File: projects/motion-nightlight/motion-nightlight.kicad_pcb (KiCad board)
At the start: 2 copper layers, 48 x 50 mm, 19 parts, among them Q1 DARK_NPN_EBC, Q2 LED_CONTROL_NPN, SW1 SW_Push, SW2 SENSOR, SW3 MODE, U1 74HC14, U2 74LS08

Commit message: clean ERC and DRC
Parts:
- moved LED1 26.8 mm to (156.5, 72.0)
- moved C1 23.0 mm to (154.0, 107.5), turned to -90 degrees
- moved SW1 22.9 mm to (158.8, 94.2), turned to -90 degrees
- moved R1 15.9 mm to (117.0, 99.5), turned to 0 degrees
- moved C2 15.7 mm to (159.0, 107.5), turned to -90 degrees
- moved LDR1 8.70 mm to (117.0, 94.5), turned to 0 degrees
- moved R2 8.40 mm to (117.0, 104.6), turned to 0 degrees
- moved R_B1 7.00 mm to (138.0, 77.3), turned to 90 degrees
- moved R_PD1 6.98 mm to (130.5, 77.3), turned to 90 degrees
- moved R3 5.68 mm to (124.7, 109.7)
- moved RV1 4.01 mm to (123.4, 89.5)
- moved PIR1 4.00 mm to (145.5, 82.9)
- moved SW3 3.20 mm to (156.2, 83.5)
- moved U1 1.63 mm to (129.2, 94.4)
- moved U2 1.63 mm to (141.7, 94.4)
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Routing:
- net /LED_ON: track 66.7 -> 9.89 mm
- net +3.3V: track 179.4 -> 156.1 mm
- net /AND_ON: track 21.1 -> 33.6 mm
- net /DARK_RAW: track 39.6 -> 27.3 mm
- net /SENSOR_DIG: track 23.3 -> 34.4 mm
- net Net-(Q1-B): track 26.3 -> 34.0 mm
- net /MOTION_RAW: track 9.38 -> 12.8 mm
- net Net-(LDR1-Pad2): track 21.2 -> 23.6 mm
- net /MOTION_DIG: track 41.7 -> 39.5 mm
- net /DARK_DIG: track 46.5 -> 48.6 mm
- net /LIGHT_ON: track 38.1 -> 38.8 mm
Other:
- board size 48 x 50 mm -> 46.7 x 45.8 mm
- board text added: "&"
- board text added: "S"
- board text removed: "AND"
- board text removed: "SENSOR"

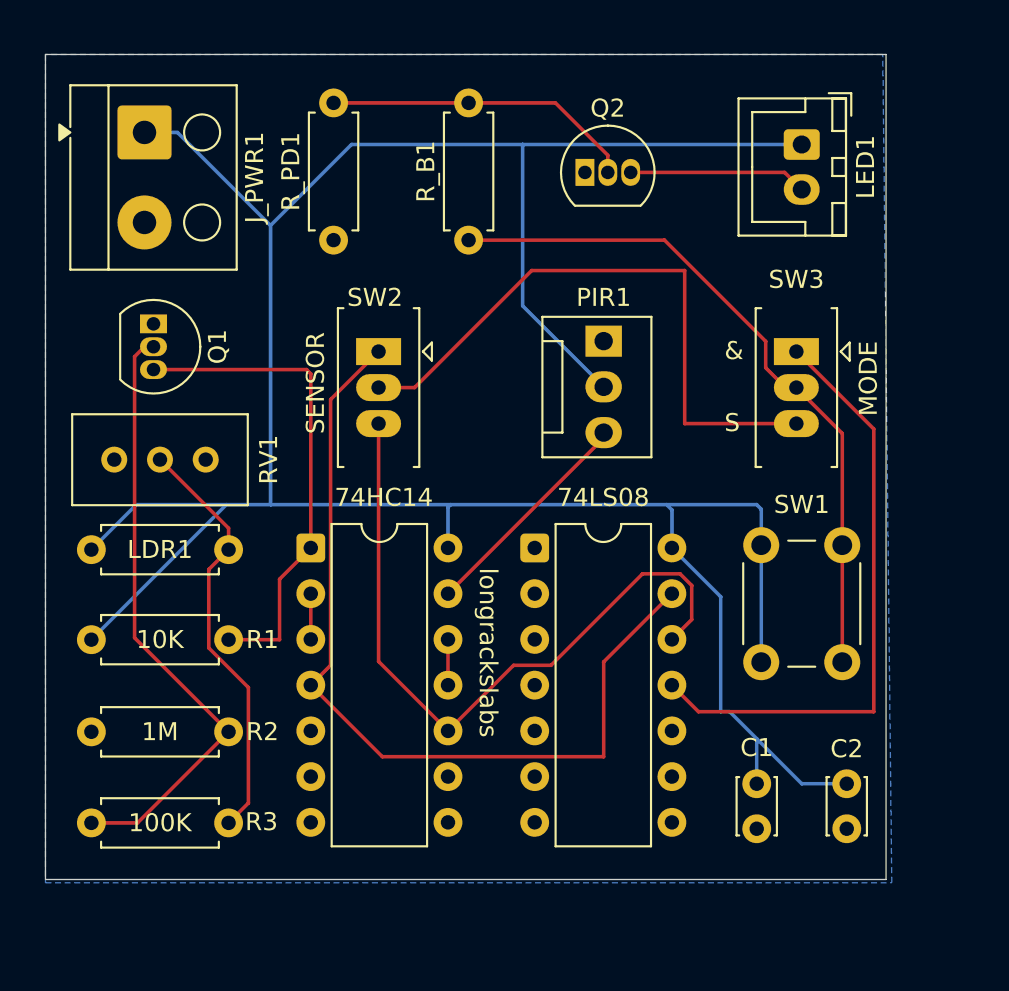
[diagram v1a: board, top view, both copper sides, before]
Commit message: layout tweaks for caps
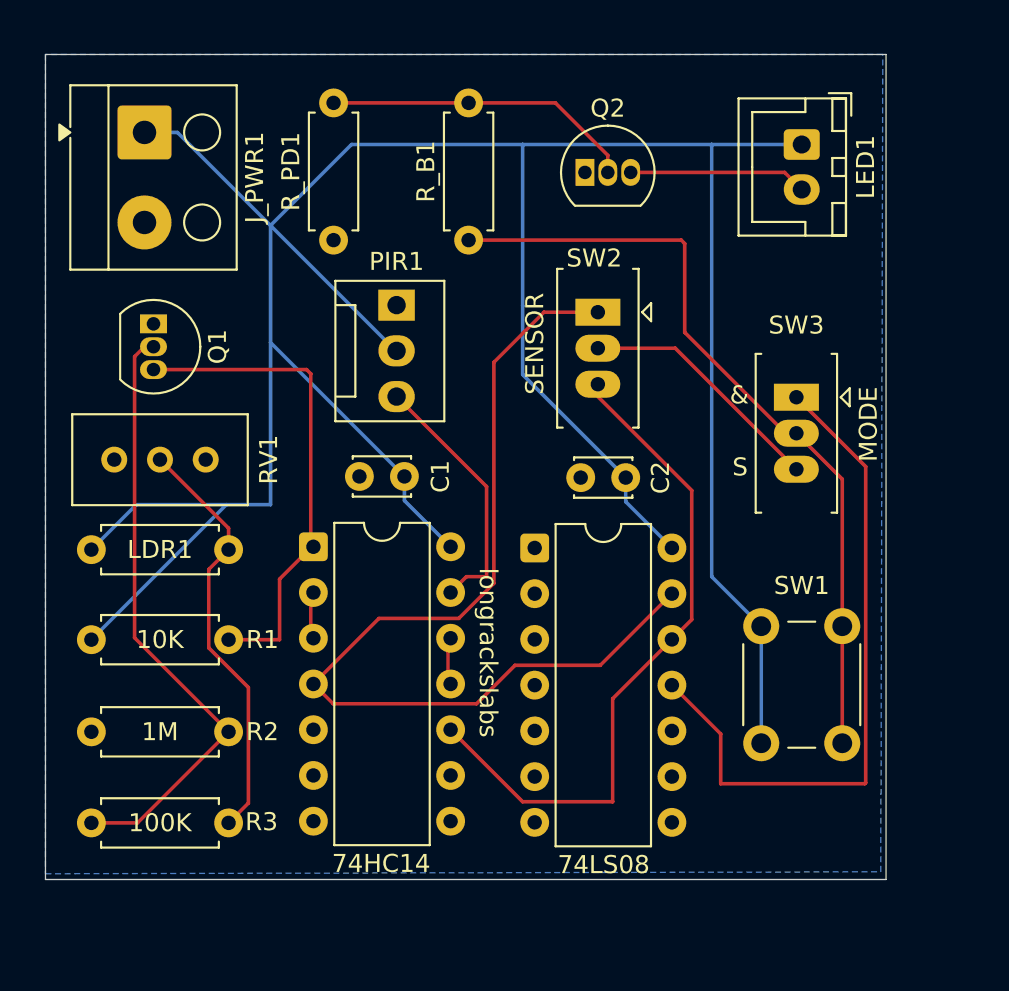
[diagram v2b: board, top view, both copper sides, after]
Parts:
- moved C1 26.0 mm to (134.4, 90.4), turned to 180 degrees
- moved C2 21.0 mm to (146.7, 90.5), turned to 180 degrees
- moved SW2 12.4 mm to (145.2, 81.3)
- moved PIR1 11.7 mm to (134.0, 80.9)
- moved SW1 4.50 mm to (158.8, 98.8)
- moved SW3 2.54 mm to (156.2, 86.0)
- moved U1 0.16 mm to (129.4, 94.3)
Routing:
- net /SENSOR_DIG: track 34.4 -> 13.8 mm
- net +3.3V: track 156.1 -> 164.1 mm
- net /DARK_DIG: track 48.6 -> 54.4 mm
- net /LIGHT_ON: track 38.8 -> 43.8 mm
- net /AND_ON: track 33.6 -> 38.3 mm
- net /MOTION_DIG: track 39.5 -> 37.1 mm
- net /MOTION_RAW: track 12.8 -> 14.7 mm

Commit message: add motion off delay
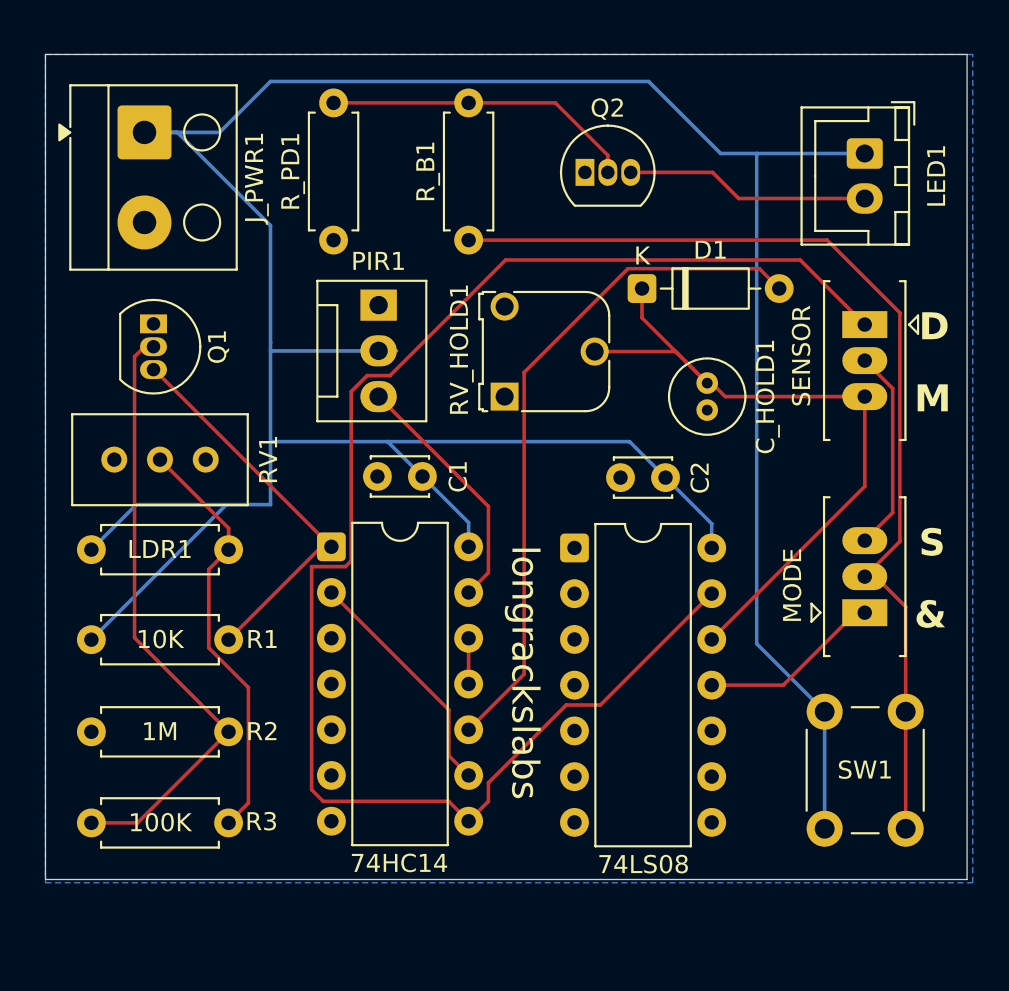
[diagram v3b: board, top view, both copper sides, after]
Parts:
- added C_HOLD1: 10uf 16V, Capacitor_THT:C_Radial_D4.0mm_H5.0mm_P1.50mm, F.Cu at (151.2, 85.2)
- added D1: 1N4148, Diode_THT:D_DO-35_SOD27_P7.62mm_Horizontal, F.Cu at (147.6, 80.0)
- added RV_HOLD1: 105, Potentiometer_THT:Potentiometer_Runtron_RM-065_Vertical, F.Cu at (140.0, 86.0)
- moved SW2 14.8 mm to (160.0, 82.0)
- moved SW3 12.6 mm to (160.0, 98.0), turned to 90 degrees
- moved SW1 5.91 mm to (162.3, 103.5)
- moved LED1 3.54 mm to (160.0, 72.5)
- moved C2 2.21 mm to (148.9, 90.5)
- moved U2 2.21 mm to (143.9, 94.4)
- moved C1 1.00 mm to (135.4, 90.4)
- moved PIR1 1.00 mm to (133.0, 80.9)
- moved U1 1.00 mm to (130.4, 94.3)
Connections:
- U1 pad 10: /MOTION_DIG -> Net-(D1-A)
- U1 pad 3: Net-(U1-Pad2) -> GND
- U1 pad 4: /DARK_DIG -> unconnected-(U1-Pad4)
- U1 pad 8: unconnected-(U1-Pad8) -> /DARK_DIG
- U1 pad 9: GND -> Net-(U1-Pad2)
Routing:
- net Net-(D1-A): track 0.00 -> 38.1 mm
- net /DARK_DIG: track 54.4 -> 87.2 mm
- net /AND_ON: track 38.3 -> 10.2 mm
- net /LIGHT_ON: track 43.8 -> 56.4 mm
- net Net-(U1-Pad2): track 2.54 -> 13.3 mm
- net +3.3V: track 164.1 -> 169.6 mm
- net /DARK_RAW: track 27.3 -> 21.9 mm
- net /LED_ON: track 9.89 -> 13.6 mm
- net /MOTION_DIG: track 37.1 -> 39.8 mm
- net /SENSOR_DIG: track 13.8 -> 11.3 mm
- net /MOTION_RAW: track 14.7 -> 13.9 mm
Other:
- board size 46.7 x 45.8 mm -> 51.2 x 45.8 mm
- board text added: "D"
- board text added: "M"

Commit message: fix up footprints and add step for trim pots
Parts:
- C_HOLD1: value 10uf 16V -> 10uf
- J_PWR1: value POWER -> - POWER +; footprint TerminalBlock_Altech:Altech_AK100_1x02_P5.00mm -> TerminalBlock_Phoenix:TerminalBlock_Phoenix_PT-1,5-2-3.5-H_1x02_P3.50mm_Horizontal
- LED1: value Conn_01x02 -> LED
- PIR1: value Conn_01x03 -> PIR
- Q1: value DARK_NPN_EBC -> DARK ON
- Q2: value LED_CONTROL_NPN -> LED ON
- RV1: value R_Trim -> DARK TRIM; footprint Potentiometer_THT:Potentiometer_Bourns_3296W_Vertical -> Potentiometer_THT:Potentiometer_Runtron_RM-065_Vertical
- RV_HOLD1: value 105 -> MOTION TRIM
- SW1: value SW_Push -> LAMP TEST
- moved R3 12.3 mm to (124.7, 97.4)
- moved R1 10.2 mm to (117.0, 109.8)
- moved LDR1 7.02 mm to (117.0, 101.5)
- moved RV1 5.10 mm to (118.4, 88.8)
- moved R2 1.02 mm to (117.0, 105.6)
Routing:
- net Net-(LDR1-Pad2): track 23.6 -> 9.44 mm
- net /DARK_RAW: track 21.9 -> 32.6 mm
- net +3.3V: track 169.6 -> 177.6 mm
- net Net-(Q1-B): track 34.0 -> 27.3 mm

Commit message: final THT version
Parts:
- U2: value 74LS08 -> 74HC08
- moved SW1 22.8 mm to (162.8, 80.8)
- moved SW2 21.0 mm to (160.2, 103.0)
- moved RV_HOLD1 13.8 mm to (153.0, 81.2), turned to -90 degrees
- moved D1 8.63 mm to (139.0, 79.9), turned to -90 degrees
- moved C_HOLD1 7.44 mm to (143.9, 84.4), turned to 90 degrees
- moved SW3 2.26 mm to (160.2, 95.8)
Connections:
- SW2 pad 3: /MOTION_DIG -> /MOTION_DIG_BUF
- U1 pad 3: GND -> /MOTION_DIG
- U1 pad 4: unconnected-(U1-Pad4) -> Net-(U1-Pad4)
- U1 pad 5: GND -> Net-(U1-Pad4)
- U1 pad 6: unconnected-(U1-Pad6) -> /MOTION_DIG_BUF
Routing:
- net /DARK_DIG: track 87.2 -> 43.4 mm
- net /MOTION_DIG_BUF: track 0.00 -> 39.1 mm
- net +3.3V: track 177.6 -> 156.9 mm
- net Net-(D1-A): track 38.1 -> 18.0 mm
- net /MOTION_DIG: track 39.8 -> 59.1 mm
- net /LIGHT_ON: track 56.4 -> 43.7 mm
- net /SENSOR_DIG: track 11.3 -> 14.9 mm
- net Net-(U1-Pad4): track 0.00 -> 2.54 mm
- net Net-(U1-Pad2): track 13.3 -> 15.2 mm
- net /AND_ON: track 10.2 -> 12.0 mm
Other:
- board text removed: "&"
- board text removed: "D"
- board text removed: "M"
- board text removed: "S"

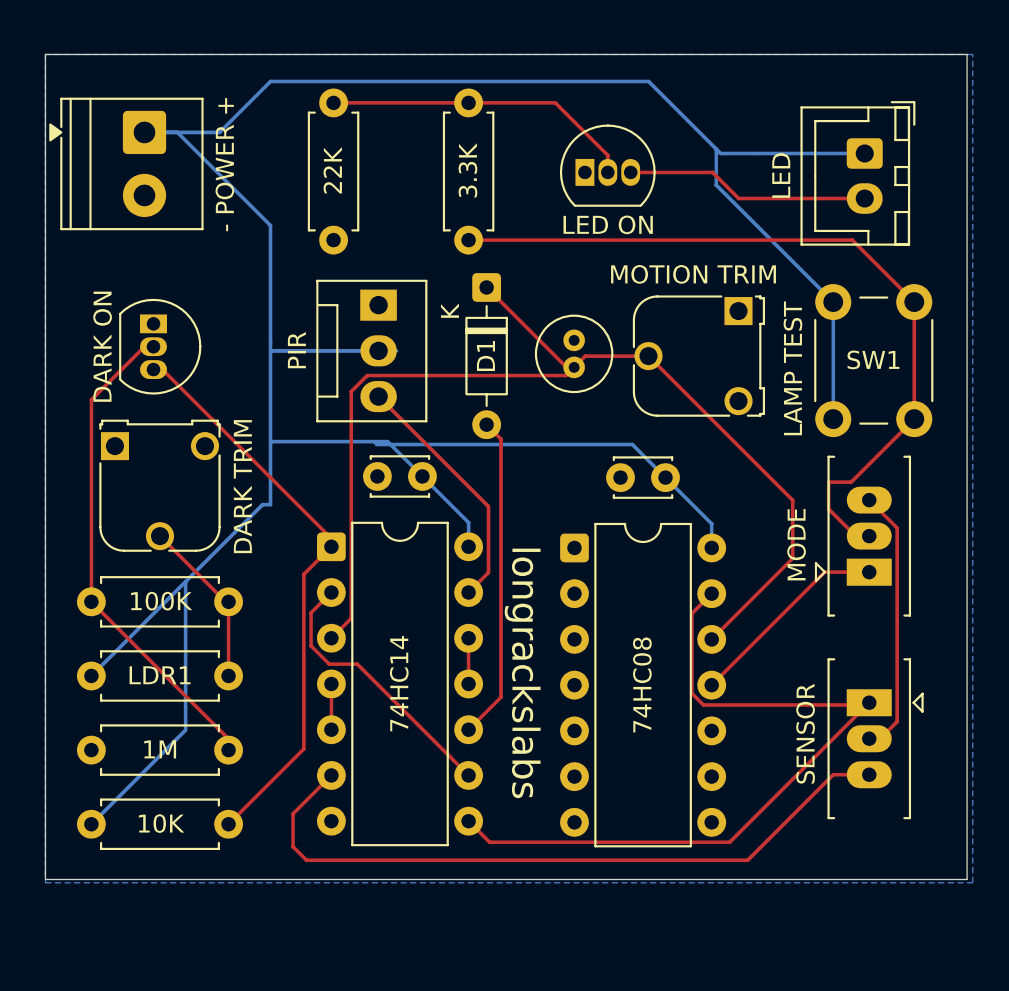
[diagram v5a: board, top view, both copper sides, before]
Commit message: SMD version ready for fab
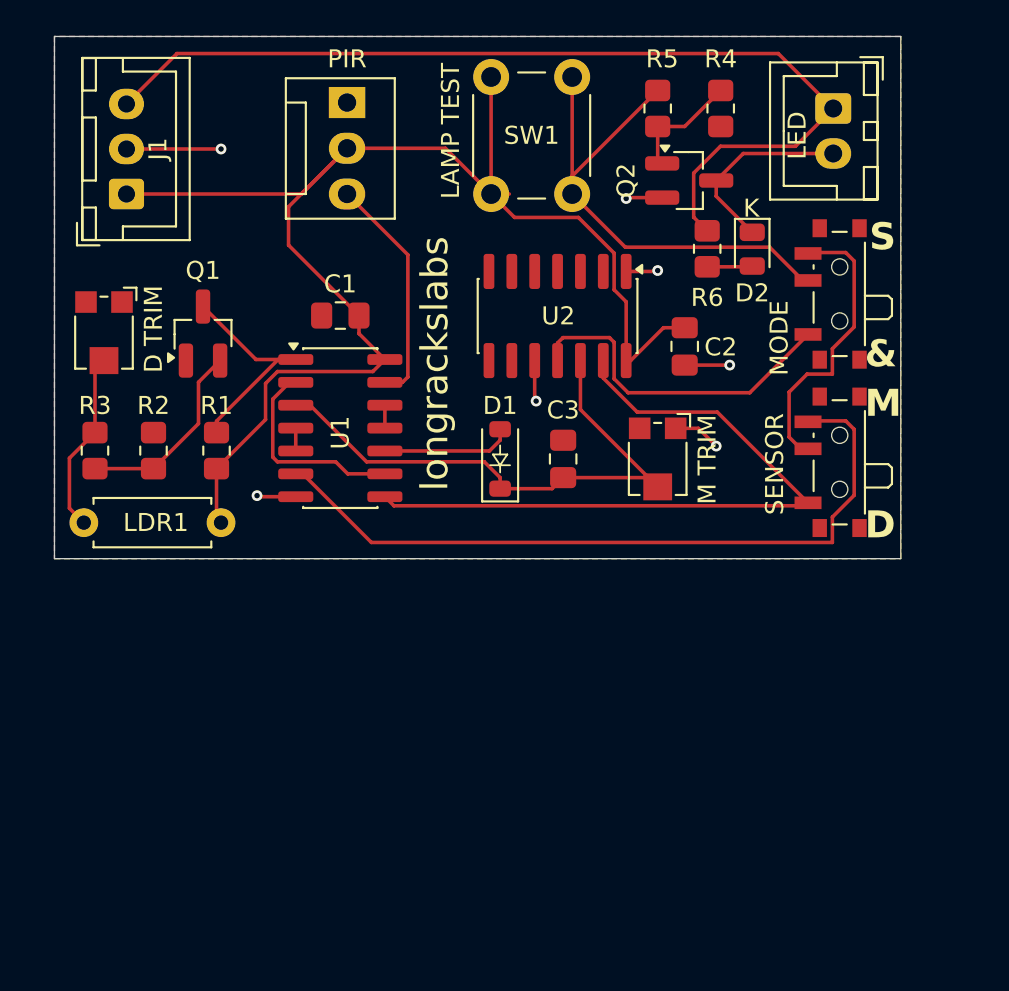
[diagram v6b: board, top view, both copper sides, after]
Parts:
- removed J_PWR1: - POWER +, TerminalBlock_Phoenix:TerminalBlock_Phoenix_PT-1,5-2-3.5-H_1x02_P3.50mm_Horizontal
- added D2: LED, LED_SMD:LED_0805_2012Metric, F.Cu at (153.8, 77.8)
- added J1: J_PWR3, Connector_JST:JST_XH_B3B-XH-A_1x03_P2.50mm_Vertical, F.Cu at (119.0, 74.8)
- added R6: 2.2K, Resistor_SMD:R_0805_2012Metric_Pad1.20x1.40mm_HandSolder, F.Cu at (151.2, 77.8)
- C1, C2: footprint Capacitor_THT:C_Disc_D3.0mm_W2.0mm_P2.50mm -> Capacitor_SMD:C_0805_2012Metric_Pad1.18x1.45mm_HandSolder
- C3: renamed from C_HOLD1; footprint Capacitor_THT:C_Radial_D4.0mm_H5.0mm_P1.50mm -> Capacitor_SMD:C_0805_2012Metric_Pad1.18x1.45mm_HandSolder
- D1: footprint Diode_THT:D_DO-35_SOD27_P7.62mm_Horizontal -> Diode_SMD:D_SOD-123
- Q1, Q2: footprint Package_TO_SOT_THT:TO-92_Inline -> Package_TO_SOT_SMD:SOT-23_Handsoldering
- R1, R2, R3: footprint Resistor_THT:R_Axial_DIN0207_L6.3mm_D2.5mm_P7.62mm_Horizontal -> Resistor_SMD:R_0805_2012Metric_Pad1.20x1.40mm_HandSolder
- R4: renamed from R_PD1; value 22K -> 100K; footprint Resistor_THT:R_Axial_DIN0207_L6.3mm_D2.5mm_P7.62mm_Horizontal -> Resistor_SMD:R_0805_2012Metric_Pad1.20x1.40mm_HandSolder
- R5: renamed from R_B1; value 3.3K -> 1K; footprint Resistor_THT:R_Axial_DIN0207_L6.3mm_D2.5mm_P7.62mm_Horizontal -> Resistor_SMD:R_0805_2012Metric_Pad1.20x1.40mm_HandSolder
- RV1: value DARK TRIM -> D TRIM; footprint Potentiometer_THT:Potentiometer_Runtron_RM-065_Vertical -> Potentiometer_SMD:Potentiometer_Bourns_TC33X_Vertical
- RV2: renamed from RV_HOLD1; value MOTION TRIM -> M TRIM; footprint Potentiometer_THT:Potentiometer_Runtron_RM-065_Vertical -> Potentiometer_SMD:Potentiometer_Bourns_TC33X_Vertical
- SW2, SW3: footprint Longracks:SW_Slide_SPDT_3pin_2.54mm -> Button_Switch_SMD:SW_SPDT_PCM12
- U1, U2: footprint Package_DIP:DIP-14_W7.62mm -> Package_SO:SOIC-14_3.9x8.7mm_P1.27mm
- moved SW1 22.7 mm to (143.8, 68.2)
- moved R4 22.7 mm to (152.0, 70.0)
- moved R1 21.9 mm to (124.0, 89.0), turned to 90 degrees
- moved R2 17.0 mm to (120.5, 89.0), turned to -90 degrees
- moved SW3 15.6 mm to (158.3, 80.3)
- moved SW2 13.5 mm to (158.3, 89.7), turned to 90 degrees
- moved U2 12.9 mm to (142.9, 81.5), turned to -90 degrees
- moved R5 12.8 mm to (148.5, 70.0), turned to -90 degrees
- moved PIR1 11.4 mm to (131.2, 69.7)
- moved R3 11.2 mm to (117.2, 89.0), turned to -90 degrees
- moved LDR1 11.2 mm to (124.2, 93.0), turned to 180 degrees
- moved C1 10.0 mm to (130.9, 81.5)
- moved D1 9.55 mm to (139.8, 89.5), turned to 90 degrees
- moved RV2 9.45 mm to (148.5, 89.6)
- moved C2 7.36 mm to (150.0, 83.2), turned to -90 degrees
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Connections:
- net /LED_ON renamed /LED_ON-
- C1 pad 1: +3.3V -> V_CONTROL
- C2 pad 1: +3.3V -> V_CONTROL
- LDR1 pad 1: +3.3V -> V_CONTROL
- LED1 pad 1: +3.3V -> V_LED+
- PIR1 pad 2: +3.3V -> V_CONTROL
- Q2 pad 1: GND -> Net-(Q2-G)
- Q2 pad 2: Net-(Q2-B) -> GND
- R1 pad 1: +3.3V -> V_CONTROL
- R4 pad 2: Net-(Q2-B) -> Net-(Q2-G)
- R5 pad 2: Net-(Q2-B) -> Net-(Q2-G)
- SW1 pad 2: +3.3V -> V_CONTROL
- U1 pad 14: +3.3V -> V_CONTROL
- U2 pad 14: +3.3V -> V_CONTROL
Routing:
- net +3.3V: track 156.9 -> 0.00 mm
- net V_CONTROL: track 0.00 -> 79.7 mm
- net V_LED+: track 0.00 -> 54.4 mm
- net /MOTION_DIG: track 59.1 -> 31.6 mm
- net /DARK_RAW: track 32.1 -> 12.8 mm
- net GND: track 0.00 -> 18.7 mm, vias 0 -> 7
- net Net-(Q2-B): track 17.4 -> 0.00 mm
- net Net-(Q1-B): track 27.3 -> 10.8 mm
- net /LIGHT_ON: track 43.7 -> 29.7 mm
- net Net-(D1-A): track 18.0 -> 7.26 mm
- net /AND_ON: track 12.0 -> 18.8 mm
- net Net-(Q2-G): track 0.00 -> 6.48 mm
- net /DARK_DIG: track 43.4 -> 39.0 mm
- net Net-(U1-Pad2): track 15.2 -> 11.5 mm
- net Net-(D2-A): track 0.00 -> 2.87 mm
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- added copper zone on F.Cu, net GND
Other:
- board size 51.2 x 45.8 mm -> 47 x 29 mm
- board text added: "&"
- board text added: "D"
- board text added: "K"
- board text added: "M"
- board text added: "S"
